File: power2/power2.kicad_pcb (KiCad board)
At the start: 2 copper layers, 49 x 44 mm, 42 parts, among them P1 CN3 from HL, P2 CONN_01X02, P3 CONN_01X03, P4 CONN_02X06, P5 CONN_01X02, P6 CONN_01X08, U1 ADC78H90CIMT, U2 Oki 5V Reg, U3 Oki 3.3V Reg, U4 LMC6482A

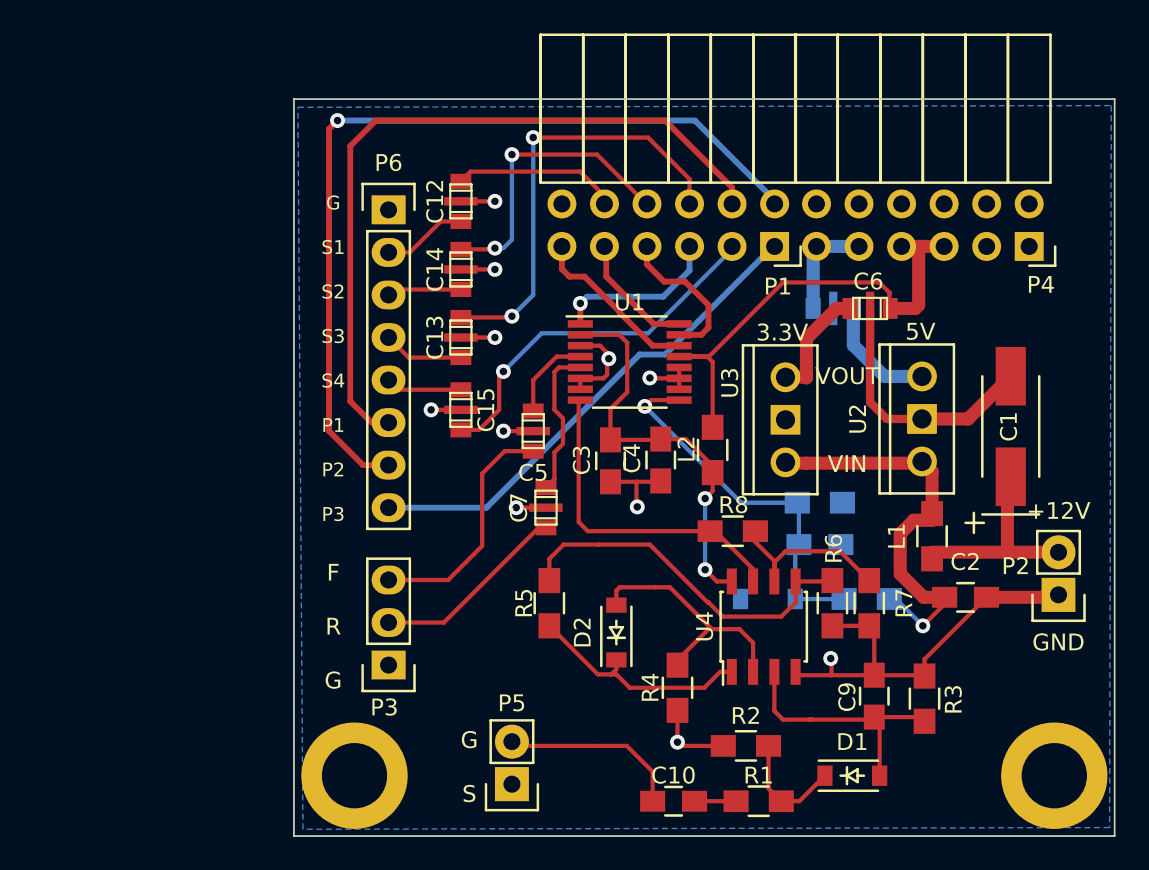
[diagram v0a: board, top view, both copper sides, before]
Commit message: Updates for v1.1 amp and V1.4 ADC
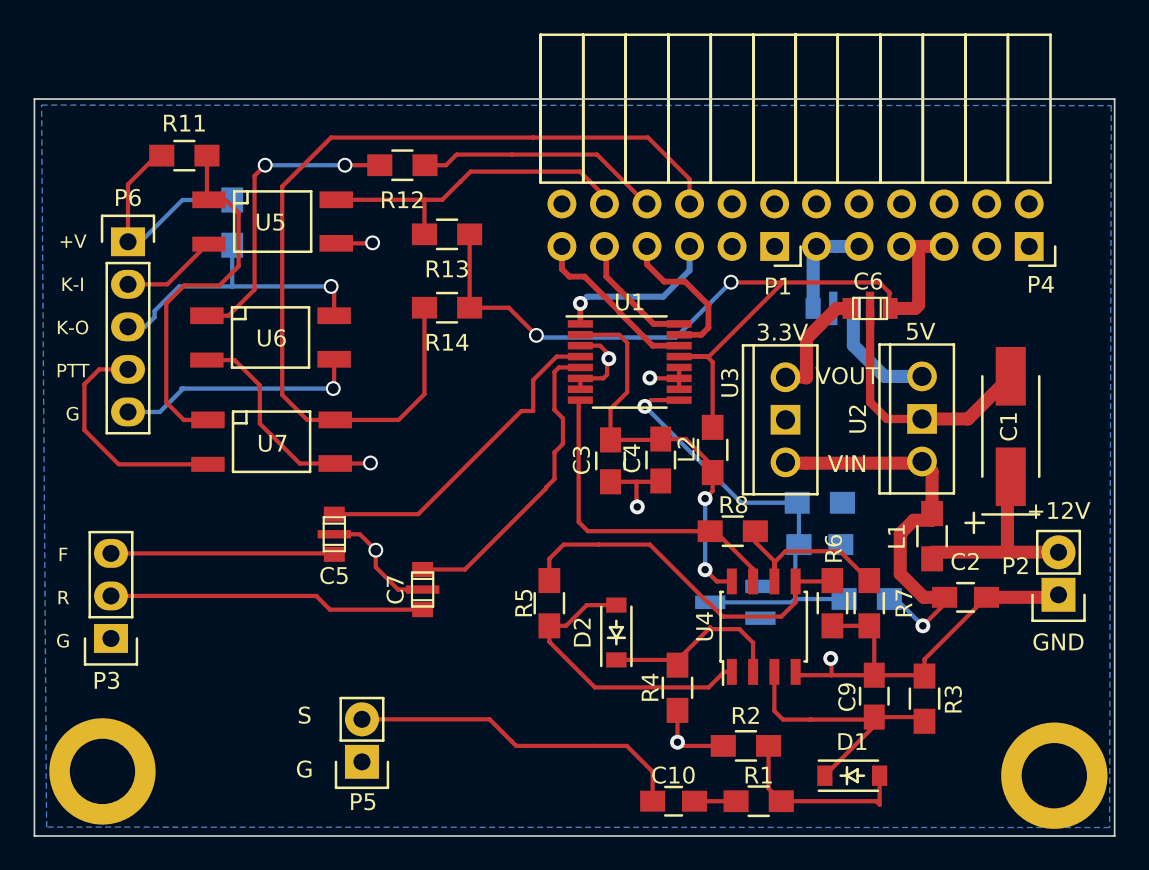
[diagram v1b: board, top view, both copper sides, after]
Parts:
- removed C12, C13, C14, C15: NFM21PC224R1C3D, SMDCAP:cfeed_0805
- added R11: 1k, Resistors_SMD:R_0805_HandSoldering, F.Cu at (108.5, 99.4)
- added R12: 270, Resistors_SMD:R_0805_HandSoldering, F.Cu at (121.5, 99.9)
- added R13: 10k, Resistors_SMD:R_0805_HandSoldering, F.Cu at (124.1, 104.1)
- added R14: 10k, Resistors_SMD:R_0805_HandSoldering, F.Cu at (124.1, 108.5)
- added R15: 10k, Resistors_SMD:R_0805_HandSoldering, B.Cu at (111.3, 103.4)
- added U5: LTV356, Opto-Devices:Optocoupler_SMD_HandSoldering_KPC357_LTV35x_PC357_SingleChannel, F.Cu at (113.7, 103.3)
- added U6: LTV356, Opto-Devices:Optocoupler_SMD_HandSoldering_KPC357_LTV35x_PC357_SingleChannel, F.Cu at (113.6, 110.2)
- added U7: LTV356, Opto-Devices:Optocoupler_SMD_HandSoldering_KPC357_LTV35x_PC357_SingleChannel, F.Cu at (113.7, 116.5)
- D3: value BZX84C 3V3 -> ZENER-SOT23-3; footprint Diodes_SMD:SOD-123 -> TO_SOT_Packages_SMD:SOT-23_Handsoldering
- P6: value CONN_01X08 -> CONN_01X05; footprint Pin_Headers:Pin_Header_Straight_1x08 -> Pin_Headers:Pin_Header_Straight_1x05
- moved P3 16.6 mm to (104.1, 128.2)
- moved P6 15.7 mm to (105.1, 104.5)
- moved MH 15.1 mm to (103.6, 136.1)
- moved C5 13.4 mm to (117.4, 122.0)
- moved P5 9.05 mm to (119.1, 135.6)
- moved C7 8.84 mm to (122.7, 125.3)
- moved D3 1.96 mm to (141.4, 126.0), turned to 270 degrees
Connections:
- D1 pad 1: Net-(D1-Pad1) -> Net-(C9-Pad1)
- D1 pad 2: Net-(C9-Pad1) -> Net-(D1-Pad2)
- D3 pad 1: GND -> (no net)
- D3 pad 2: Net-(C11-Pad1) -> GND
- P6 pad 1: GND -> Net-(P6-Pad1)
- R1 pad 2: Net-(D1-Pad1) -> Net-(D1-Pad2)
- R2 pad 1: Net-(D1-Pad1) -> Net-(D1-Pad2)
- R4 pad 1: Net-(D2-Pad2) -> Net-(D2-Pad1)
- R5 pad 2: Net-(D2-Pad1) -> Net-(D2-Pad2)
- U4 pad 1: Net-(D2-Pad1) -> Net-(D2-Pad2)
- U4 pad 2: Net-(D2-Pad2) -> Net-(D2-Pad1)
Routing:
- net Net-(P1-Pad2): track 51.8 -> 0.58 mm, vias 1 -> 0
- net Net-(P1-Pad4): track 44.1 -> 0.00 mm
- net Net-(P1-Pad1): track 29.5 -> 0.09 mm
- net Net-(P1-Pad6): track 26.1 -> 55.4 mm, vias 2 -> 0
- net Net-(C6-Pad2): track 29.9 -> 55.1 mm, vias 0 -> 2
- net Net-(R11-Pad1): track 0.00 -> 22.0 mm
- net Net-(P1-Pad3): track 22.0 -> 0.17 mm, vias 1 -> 0
- net Net-(R12-Pad2): track 0.00 -> 18.0 mm, vias 0 -> 2
- net Net-(C5-Pad1): track 5.24 -> 19.7 mm
- net Net-(P6-Pad1): track 0.00 -> 13.7 mm
- net Net-(P6-Pad3): track 4.45 -> 17.9 mm, vias 0 -> 1
- net GND: track 69.8 -> 81.5 mm, vias 11 -> 8
- net Net-(D1-Pad2): track 0.00 -> 11.3 mm
- net Net-(P6-Pad5): track 4.56 -> 14.8 mm, vias 0 -> 1
- net Net-(P1-Pad10): track 9.89 -> 19.9 mm
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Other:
- board size 49 x 44 mm -> 64.5 x 44 mm
- board text added: "+V K-I K-O PTT G"
- board text added: "Hermes Lite ADC I/O and Pwr © 2016 W9JSW ver 1.4"
- board text added: "S G"
- board text removed: "G S"
- board text removed: "G S1 S2 S3 S4 P1 P2 P3"
- board text removed: "Hermes Lite ADC I/O and Pwr © 2015 W9JSW ver 1.2"
